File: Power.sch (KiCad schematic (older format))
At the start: 32 parts

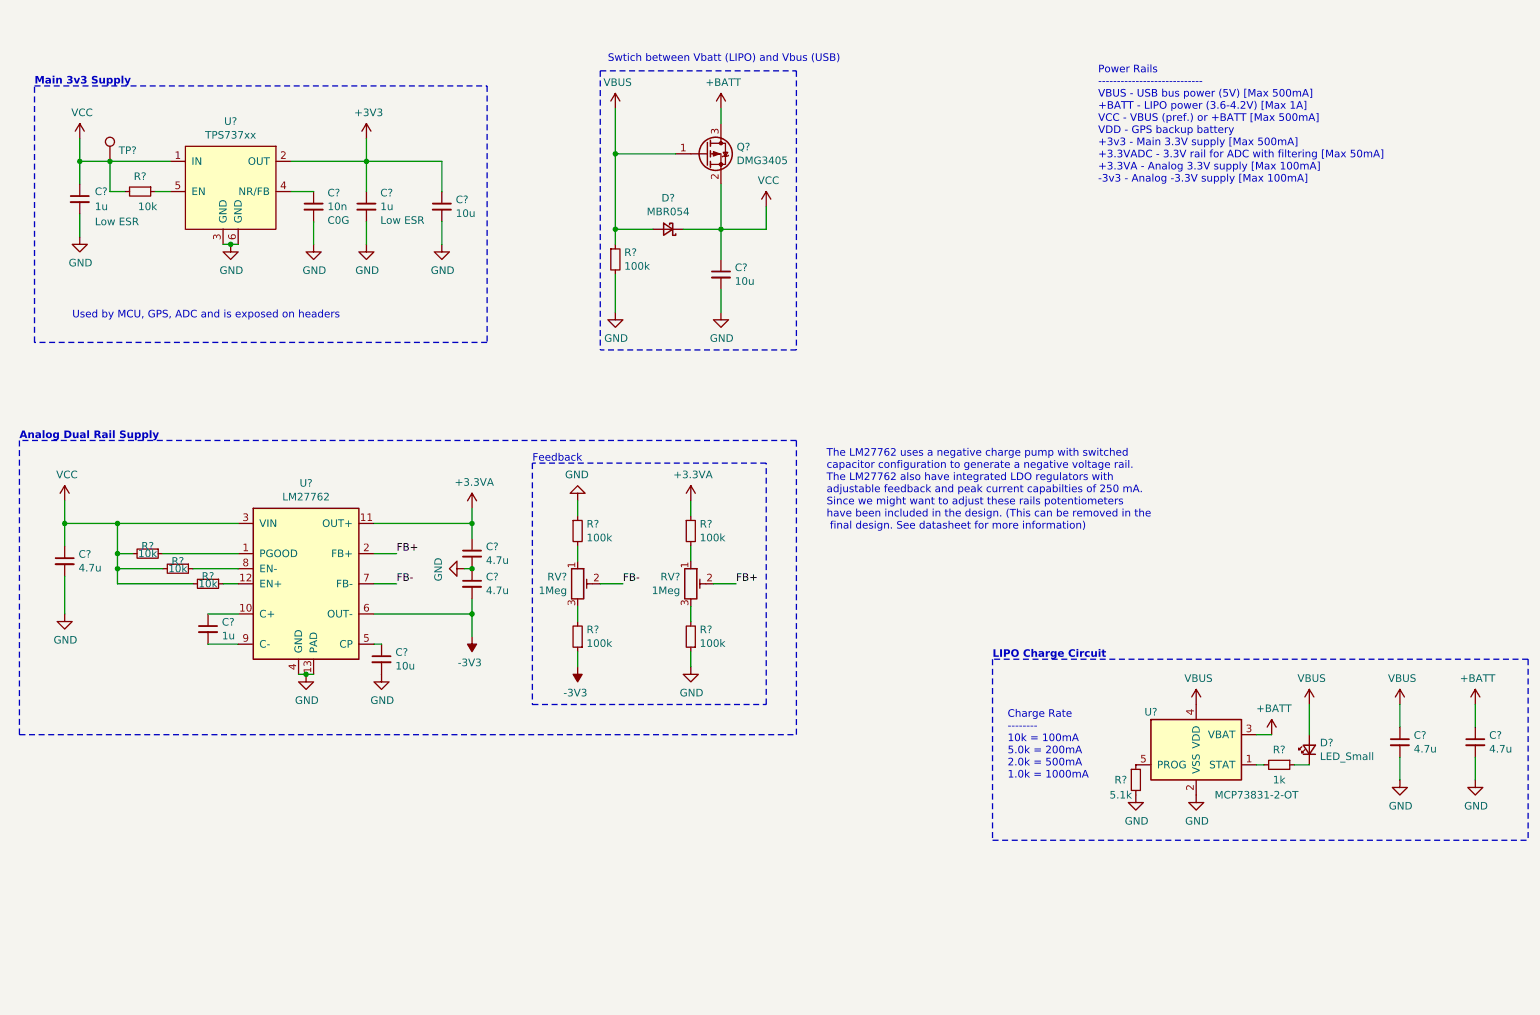
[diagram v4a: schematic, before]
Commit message: Change Connector Layout
Also add Mic. board to connectors
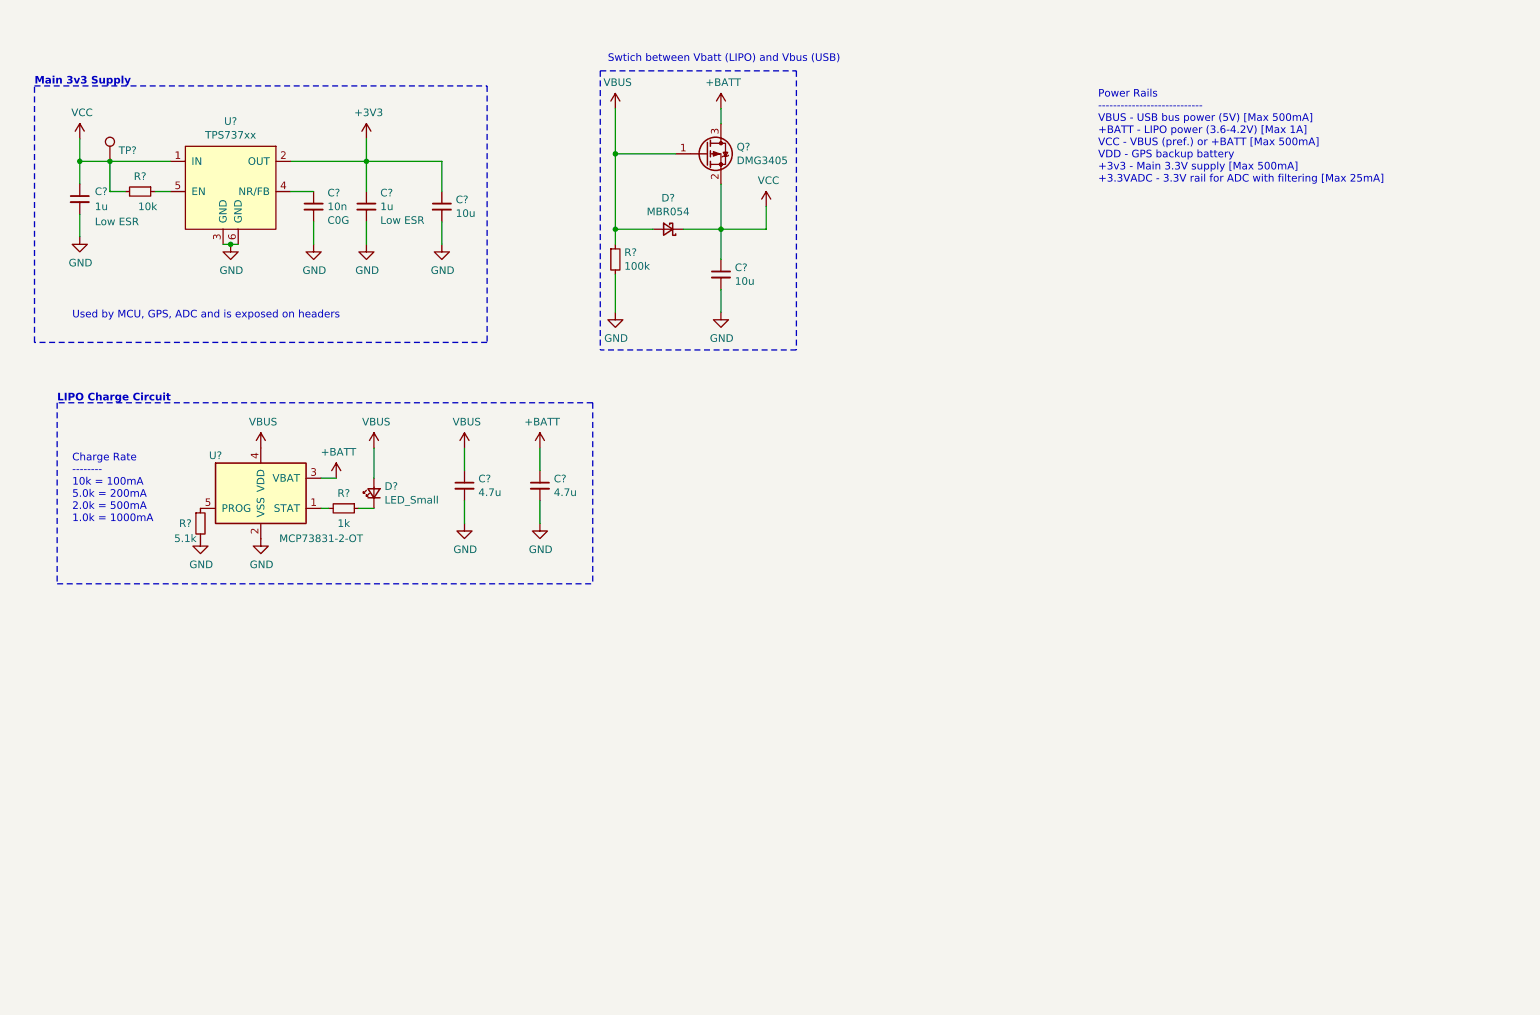
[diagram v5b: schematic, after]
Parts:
- removed C? (x3): 4.7u, symbol Device:C_Small
- removed C?: 1u, symbol Device:C_Small
- removed C?: 10u, symbol Device:C_Small
- removed R? (x4): 100k, symbol Device:R_Small
- removed R? (x3): 10k, symbol Device:R_Small
- removed RV? (x2): 1Meg, symbol Device:R_POT_TRIM
- removed U?: LM27762, Package_SON:WSON-12-1EP_3x2mm_P0.5mm_EP1x2.65_ThermalVias, symbol Regulator_SwitchedCapacitor:LM27762
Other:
- note added: "Power Rails\n----------------------------\nVBUS - USB bus power (5V) [Max 500mA]\n+BATT - LIPO power (3.6-4.2V) [Max 1A]\nVCC - VBUS (pref.) or +BATT [Max 500mA]\nVDD - GPS backup battery\n+3v3 - Main 3.3V supply [Max 500mA]\n+3.3VADC - 3.3V rail for ADC with filtering [Max 25mA]"
- note removed: "Analog Dual Rail Supply"
- note removed: "Feedback"
- note removed: "Power Rails\n----------------------------\nVBUS - USB bus power (5V) [Max 500mA]\n+BATT - LIPO power (3.6-4.2V) [Max 1A]\nVCC - VBUS (pref.) or +BATT [Max 500mA]\nVDD - GPS backup battery\n+3v3 - Main 3.3V supply [Max 500mA]\n+3.3VADC - 3.3V rail for ADC with filtering [Max 50mA]\n+3.3VA - Analog 3.3V supply [Max 100mA]\n-3v3 - Analog -3.3V supply [Max 100mA]"
- note removed: "The LM27762 uses a negative charge pump with switched \ncapacitor configuration to generate a negative voltage rail. \nThe LM27762 also have integrated LDO regulators with \nadjustable feedback and peak current capabilties of 250 mA. \nSince we might want to adjust these rails potentiometers \nhave been included in the design. (This can be removed in the\n final design. See datasheet for more inf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"
- moved on the sheet: C?, D?, R?, U?

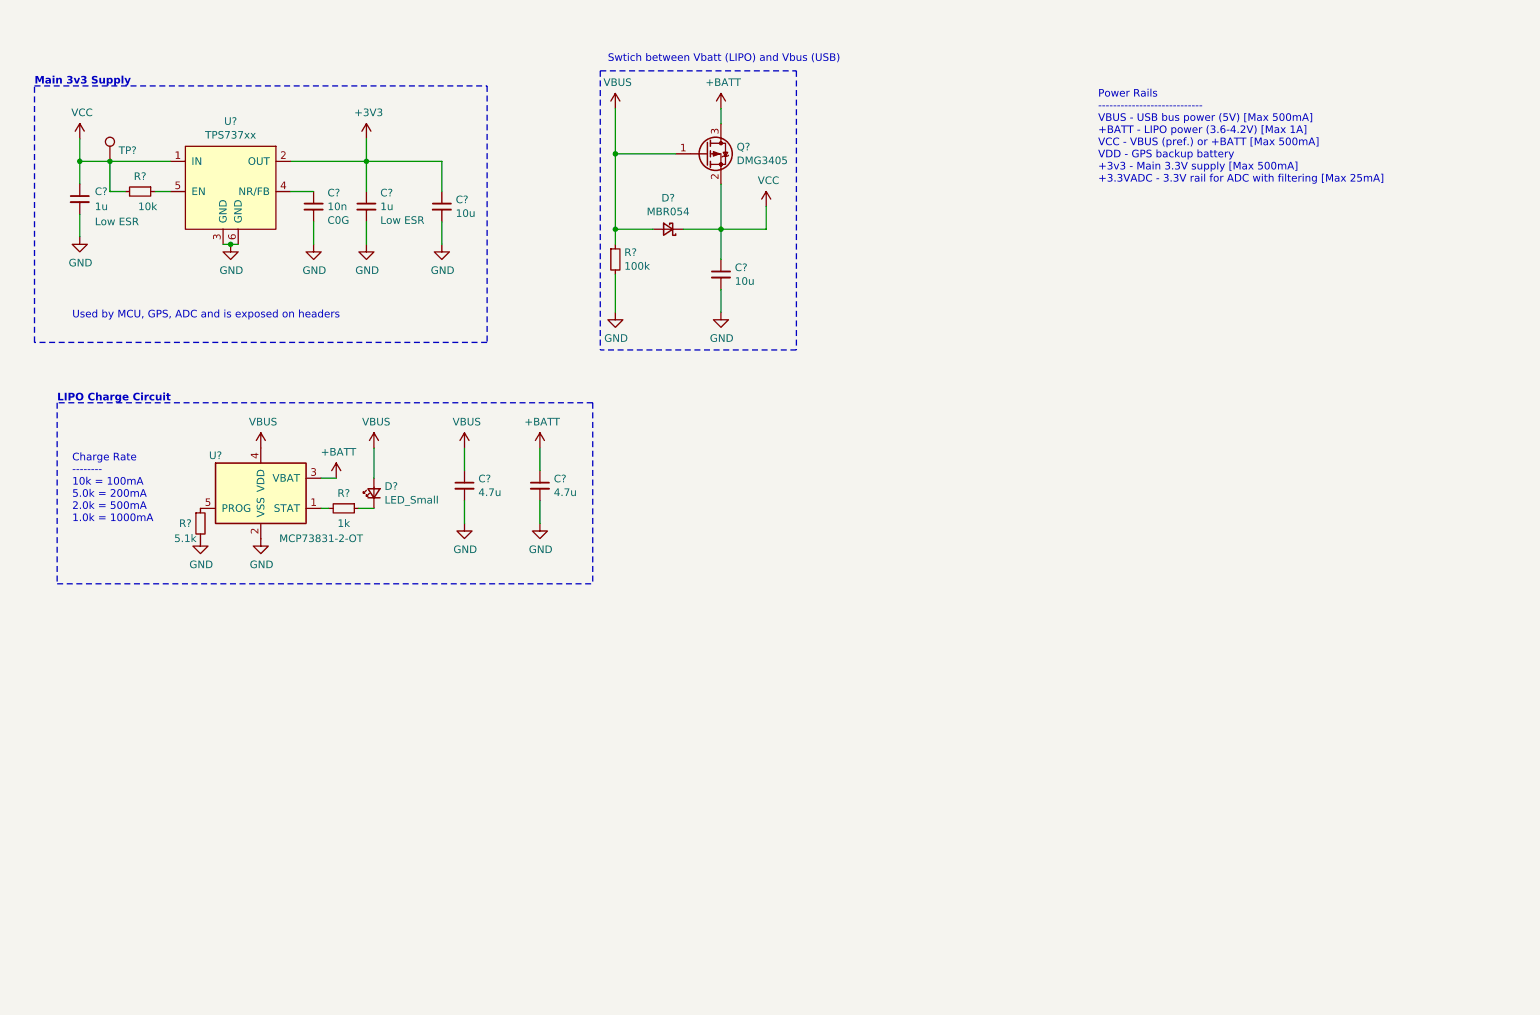
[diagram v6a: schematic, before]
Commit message: Design MCU section
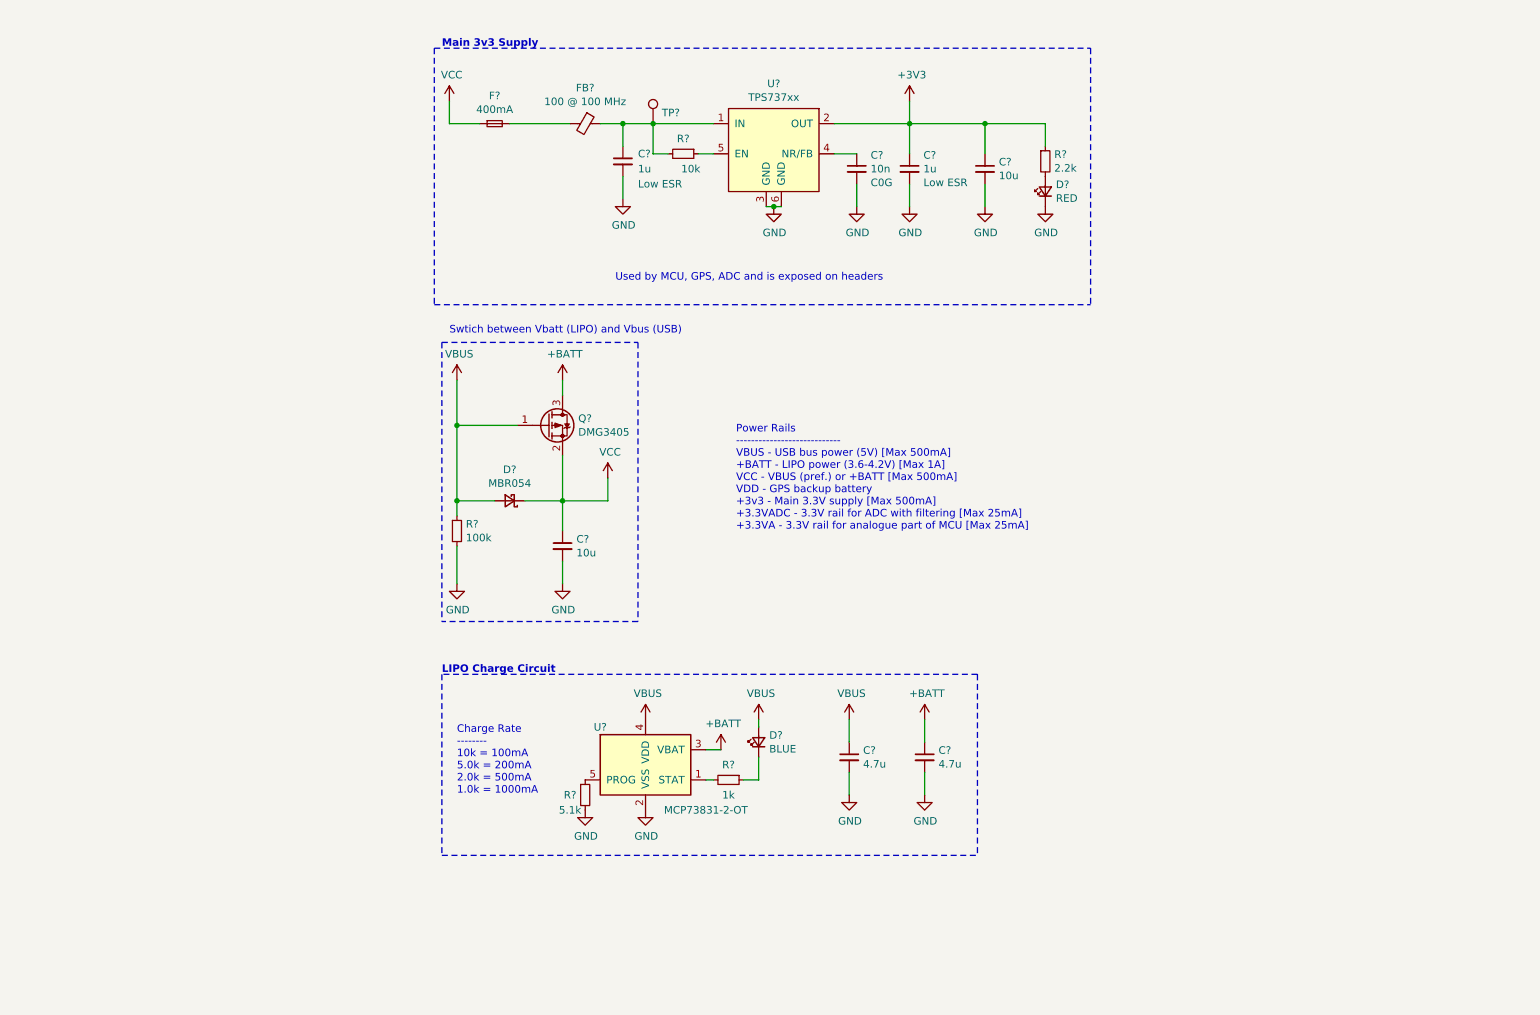
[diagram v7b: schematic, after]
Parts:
- added D?: RED, symbol Device:LED_Small
- added F?: 400mA, symbol Device:Fuse_Small
- added FB?: 100 @ 100 MHz, symbol Device:Ferrite_Bead_Small
- added R?: 2.2k, symbol Device:R_Small
- D?: value LED_Small -> BLUE
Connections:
- net +3V3: now also R?.1
- net GND: now also D?.1 (K)
- net VCC: now also F?.1; no longer C?.1, R?.2, TP?.1, U?.1 (IN)
- new net: C?.1, FB?.1, R?.2, TP?.1, U?.1 (IN)
- new net: D?.2 (A), R?.2
- new net: F?.2, FB?.2
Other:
- note added: "Power Rails\n----------------------------\nVBUS - USB bus power (5V) [Max 500mA]\n+BATT - LIPO power (3.6-4.2V) [Max 1A]\nVCC - VBUS (pref.) or +BATT [Max 500mA]\nVDD - GPS backup battery\n+3v3 - Main 3.3V supply [Max 500mA]\n+3.3VADC - 3.3V rail for ADC with filtering [Max 25mA]\n+3.3VA - 3.3V rail for analogue part of MCU [Max 25mA]"
- note removed: "Power Rails\n----------------------------\nVBUS - USB bus power (5V) [Max 500mA]\n+BATT - LIPO power (3.6-4.2V) [Max 1A]\nVCC - VBUS (pref.) or +BATT [Max 500mA]\nVDD - GPS backup battery\n+3v3 - Main 3.3V supply [Max 500mA]\n+3.3VADC - 3.3V rail for ADC with filtering [Max 25mA]"
- moved on the sheet: C?, D?, Q?, R?, TP?, U?

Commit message: Add PWR Flags
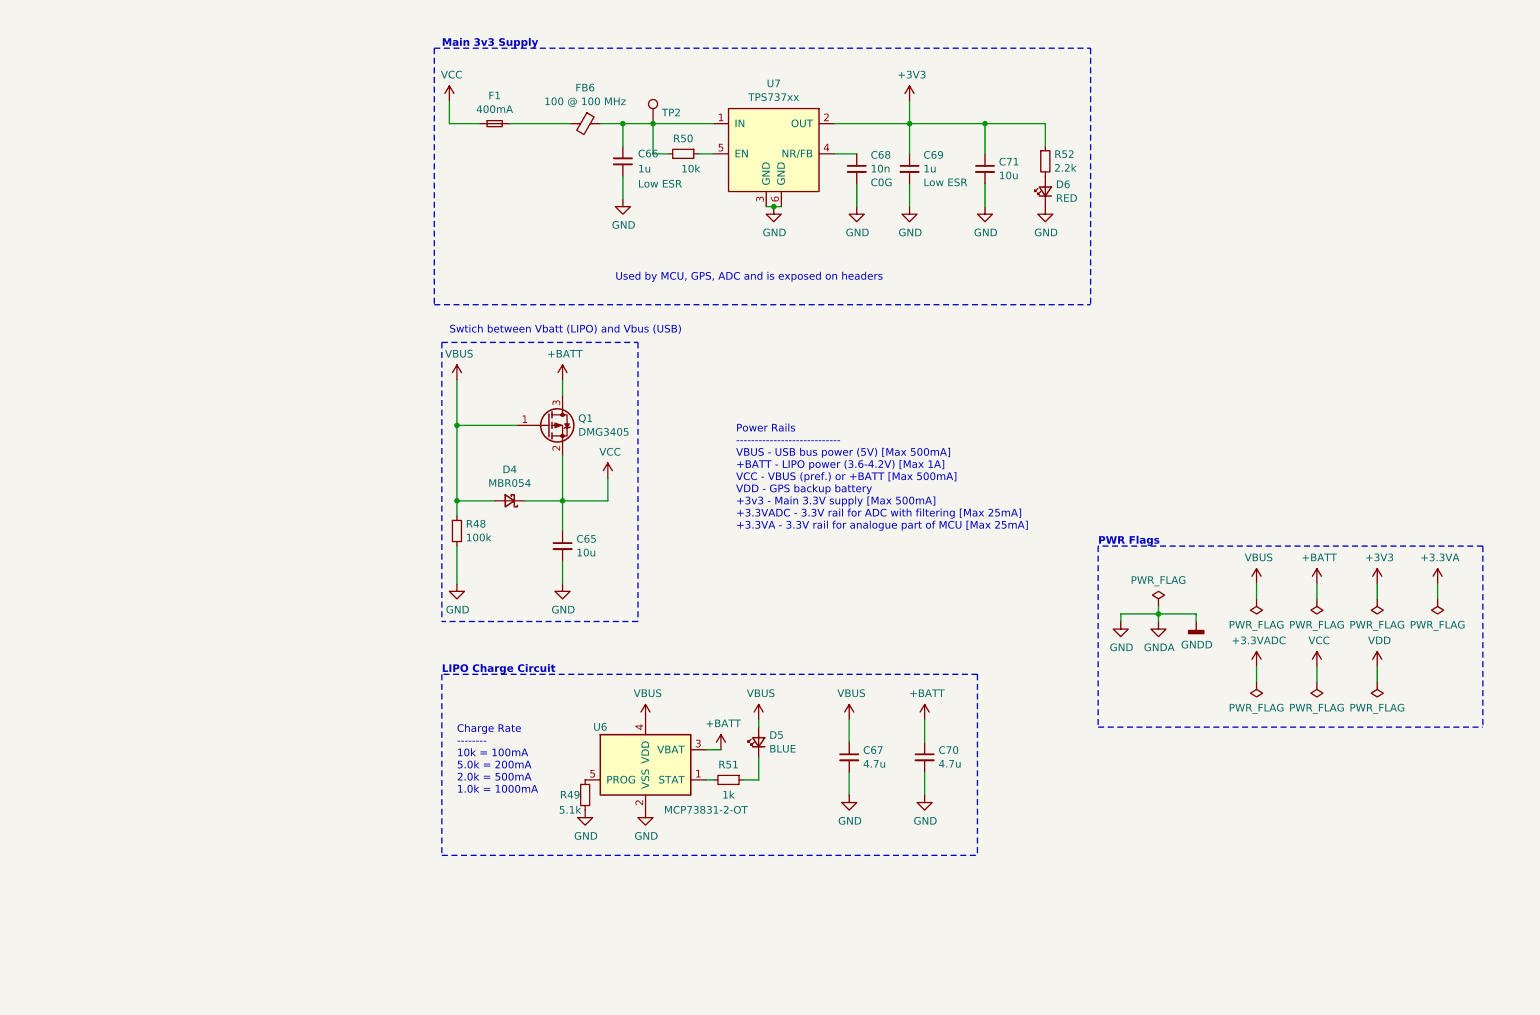
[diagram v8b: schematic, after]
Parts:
- gave numbers to parts that had none: 21
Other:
- note added: "PWR Flags"
